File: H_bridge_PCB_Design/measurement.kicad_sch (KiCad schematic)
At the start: 20 parts, among them IC5 ACS37800KMACTR-030B3-I2C, J4 TMS-102-21-G-S, J5 TMS-102-21-G-S, U4 INA228

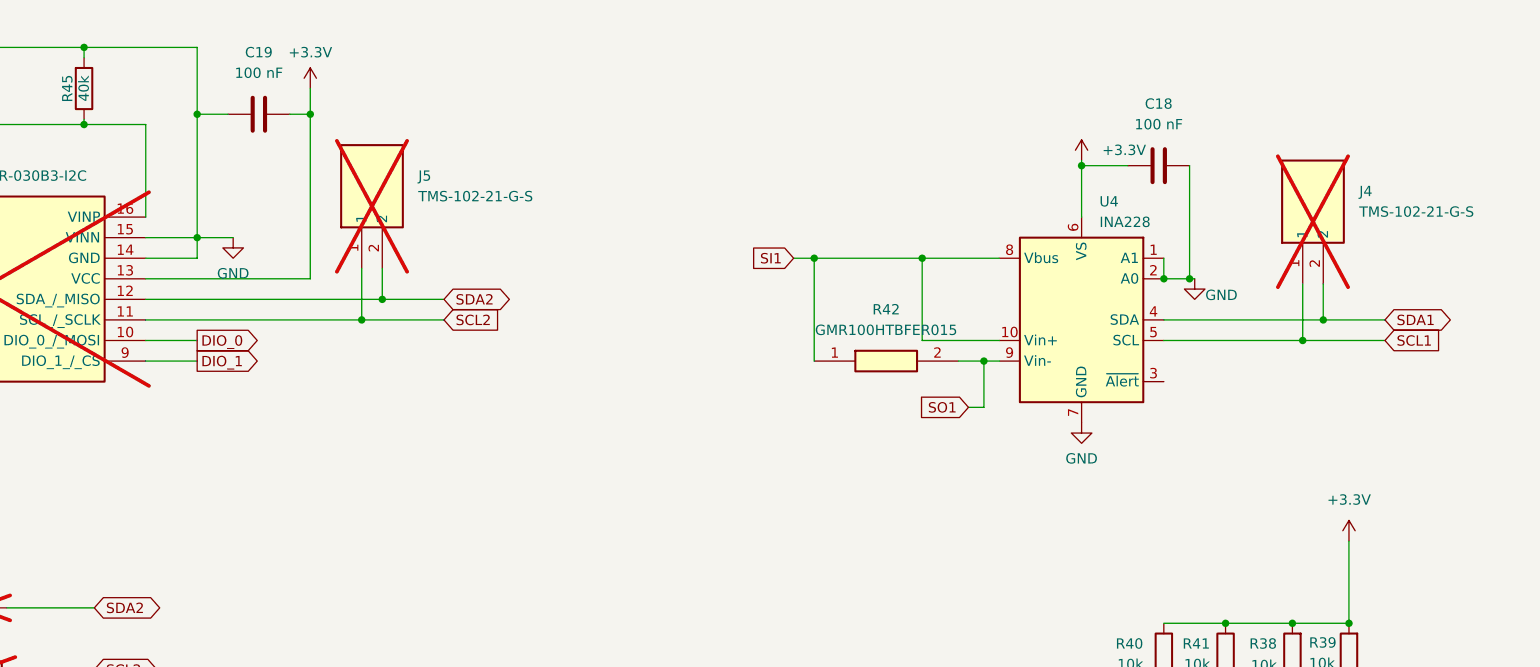
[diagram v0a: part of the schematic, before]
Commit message: Interrupt for PWM and unipolar modulation
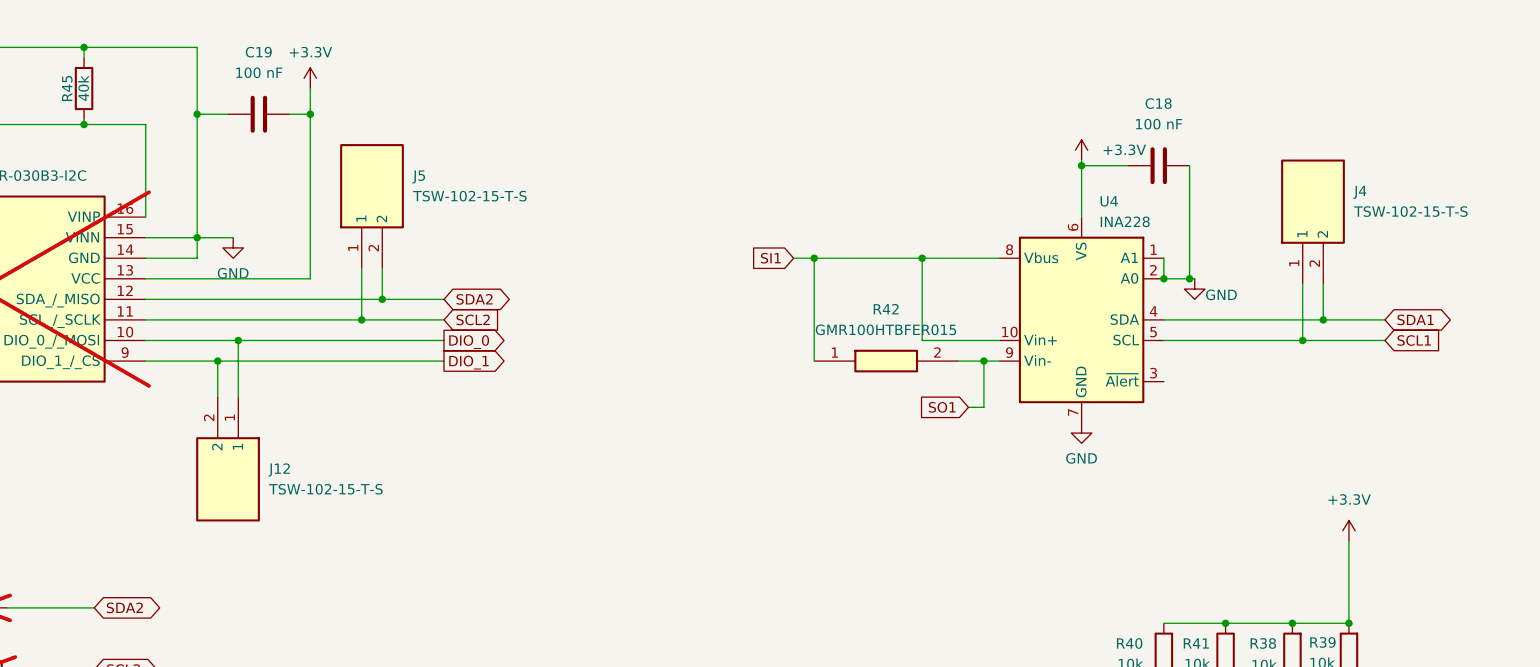
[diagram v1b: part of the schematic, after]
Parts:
- removed J4, J5: TMS-102-21-G-S, SamacSys_Parts:TMS-102-YY-XX-S, symbol SamacSys_Parts:TMS-102-21-G-S
- added J12, J4, J5: TSW-102-15-T-S, SamacSys_Parts:TSW-102-XX-YY-S, symbol SamacSys_Parts:TSW-102-15-T-S
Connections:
- net DIO_0: now also J12.1
- net DIO_1: now also J12.2
- net SCL1: now also J4.1
- net SCL2: now also J5.1
- net SDA1: now also J4.2
- net SDA2: now also J5.2

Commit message: huge changes output measurement
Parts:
- removed IC5: ACS37800KMACTR-030B3-I2C, ACS37002LMCA050U5, symbol SamacSys_Parts:ACS37800KMACTR-030B3-I2C
- removed R15, R43, R44: 1M, Resistor_SMD:R_0805_2012Metric_Pad1.20x1.40mm_HandSolder, symbol Device:R
- removed R38, R39: 10k, Resistor_SMD:R_0805_2012Metric_Pad1.20x1.40mm_HandSolder, symbol Device:R
- removed R45: 40k, Resistor_SMD:R_0805_2012Metric_Pad1.20x1.40mm_HandSolder, symbol Device:R
- removed R46, R47, R48, R49: 0, Resistor_SMD:R_0805_2012Metric_Pad1.20x1.40mm_HandSolder, symbol Device:R
- added C22, C33, C35: 100 nF, Resistor_SMD:R_0805_2012Metric_Pad1.20x1.40mm_HandSolder, symbol Device:C
- added C31, C32, C34, C36: 1 µF, Resistor_SMD:R_0805_2012Metric_Pad1.20x1.40mm_HandSolder, symbol Device:C
- added IC1, IC3: AMC1306M25DWVR, SOIC127P1150X280-8N, symbol SamacSys_Parts:AMC1306M25DWVR
- added PS1: NXJ1S0303MC-R13, NXJ1S0303MCR13, symbol SamacSys_Parts:NXJ1S0303MC-R13
- added R15: GMR100HTBFER015, Resistor_SMD:R_2512_6332Metric_Pad1.40x3.35mm_HandSolder, symbol SamacSys_Parts:GMR100HTBFER015
- added R17: 1k, Resistor_SMD:R_0805_2012Metric_Pad1.20x1.40mm_HandSolder, symbol Device:R
- C19: footprint Capacitor_SMD:C_0805_2012Metric -> Resistor_SMD:R_0805_2012Metric_Pad1.20x1.40mm_HandSolder
- R16: value 1M -> 120k; LCSC Part# C2771009 -> C84376
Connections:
- net +3.3V: now also C19.2, C22.2, C31.2, C32.2, IC1.8 (DVDD), IC3.8 (DVDD), PS1.3 (+VIN); no longer C19.1
- net GND: now also C19.1, C22.1, C31.1, C32.1, IC1.5 (DGND), IC3.5 (DGND), PS1.1 (-VIN); no longer C19.2
- net SI2: now also C33.1, C34.1, C35.1, C36.1, IC1.3 (AINN), IC1.4 (AGND), IC3.3 (AINN), IC3.4 (AGND), PS1.7 (-VOUT), R15.2, R17.2; no longer R16.2
- net SO2: now also IC3.2 (AINP), R15.1
- net SV2: now also R16.1
- net DIO_0 renamed CLK_V
- net CLK_V: now also IC1.7 (CLKIN)
- net DIO_1 renamed Data_V
- net Data_V: now also IC1.6 (DOUT)
- net SCL2 renamed Data_C
- net Data_C: now also IC3.6 (DOUT)
- net SDA2 renamed CLK_C
- net CLK_C: now also IC3.7 (CLKIN)
- new net: IC1.2 (AINP), R16.2, R17.1
- new net 3.3_Sensor: C33.2, C34.2, C35.2, C36.2, IC1.1 (AVDD), IC3.1 (AVDD), PS1.8 (+VOUT)
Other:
- moved on the sheet: J12, J5, R40, R41

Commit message: new pcb
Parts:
- added R18: 12k, Resistor_SMD:R_0805_2012Metric_Pad1.20x1.40mm_HandSolder, symbol Device:R
- added R19: 0, Resistor_SMD:R_0805_2012Metric_Pad1.20x1.40mm_HandSolder, symbol Device:R
- C18, C19, C22, C33, C35: LCSC Part # (none) -> C49678; LCSC Part# C49678 -> (none)
- C31, C32, C34, C36: LCSC Part # (none) -> C28323; LCSC Part# C49678 -> (none)
- IC1, IC3: LCSC Part # (none) -> C471874
- PS1: LCSC Part # (none) -> C6943307
- R15, R42: LCSC Part # (none) -> C2985715; LCSC Part# C2985715 -> (none)
- R16: LCSC Part # (none) -> C473315; LCSC Part# C84376 -> (none)
- R17: LCSC Part # (none) -> C95781; LCSC Part# C84376 -> (none)
- R40, R41: LCSC Part # (none) -> C84376; LCSC Part# C84376 -> (none)
- U4: LCSC Part # (none) -> C2862904; LCSC Part# C2862904 -> (none)
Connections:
- net +3.3V: now also R18.1
- net Shutoff1: now reaches U4.3 (~{Alert})
- net Shutoff1: now also R18.2, R19.2
- new net Shutoff: R19.1
